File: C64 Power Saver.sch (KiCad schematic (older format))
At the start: 16 parts, among them J1 OUTPUT, J5 DIN-7, K1 SANYOU_SRD_Form_C, Q1 PN2222A, Q2 PN2222A

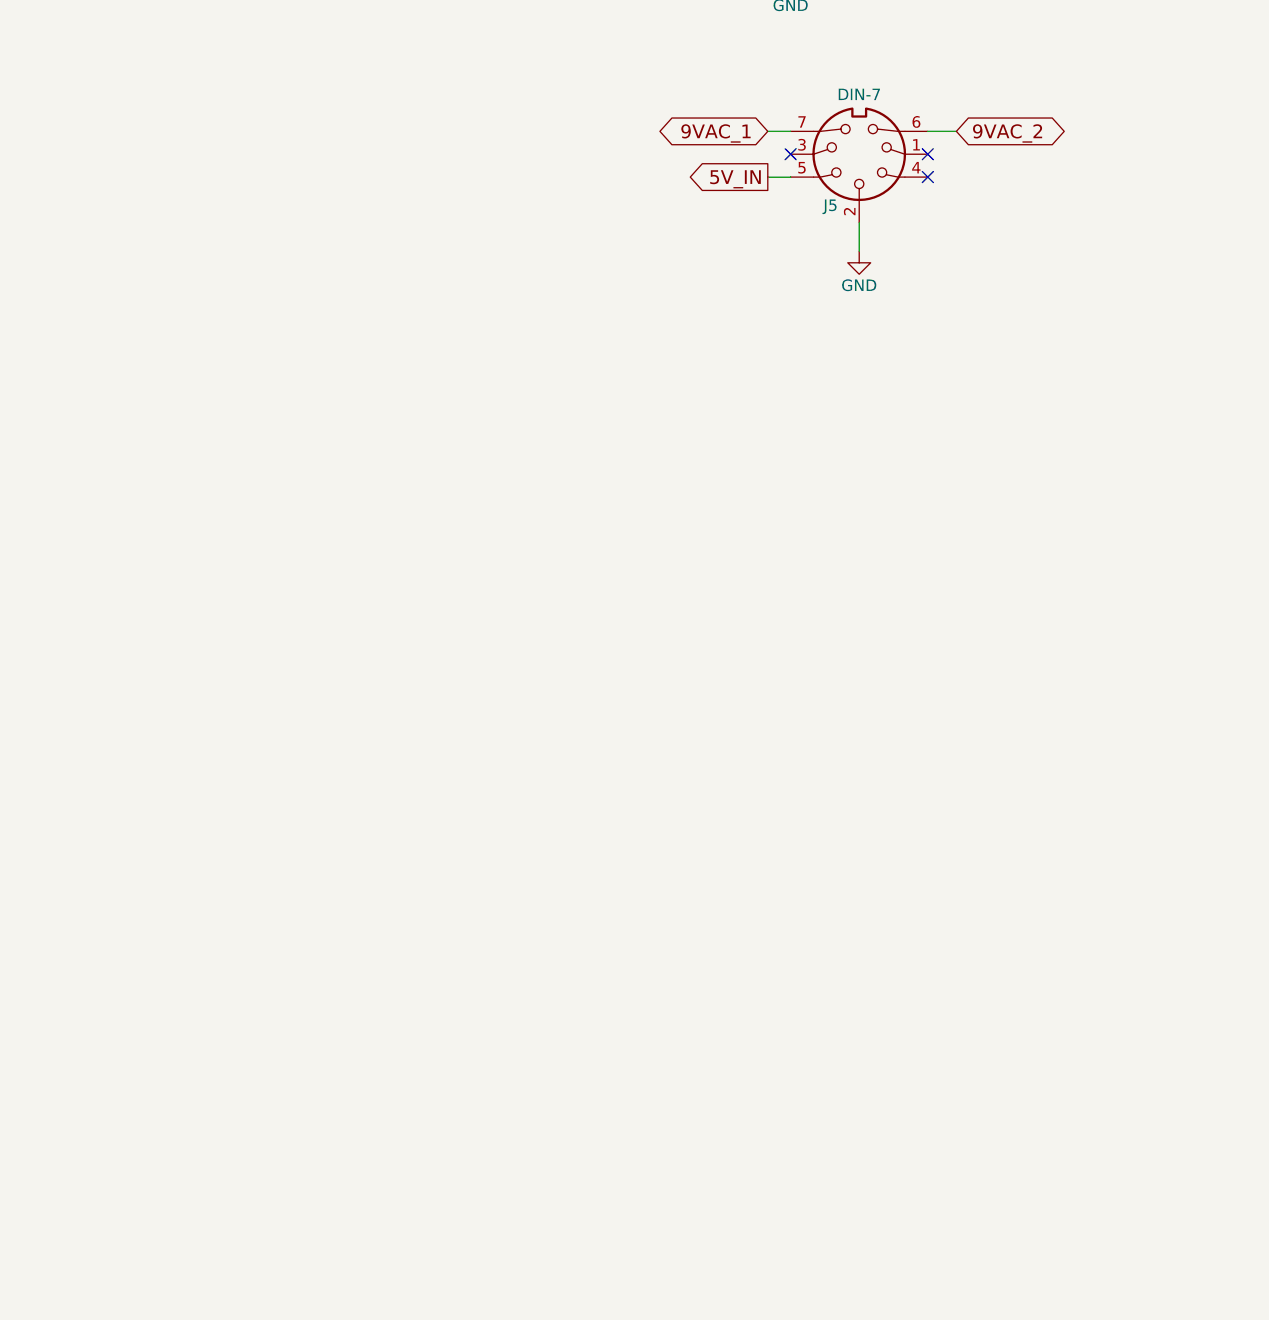
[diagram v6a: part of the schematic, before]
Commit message: Add 5v to DIN-7 pin 4
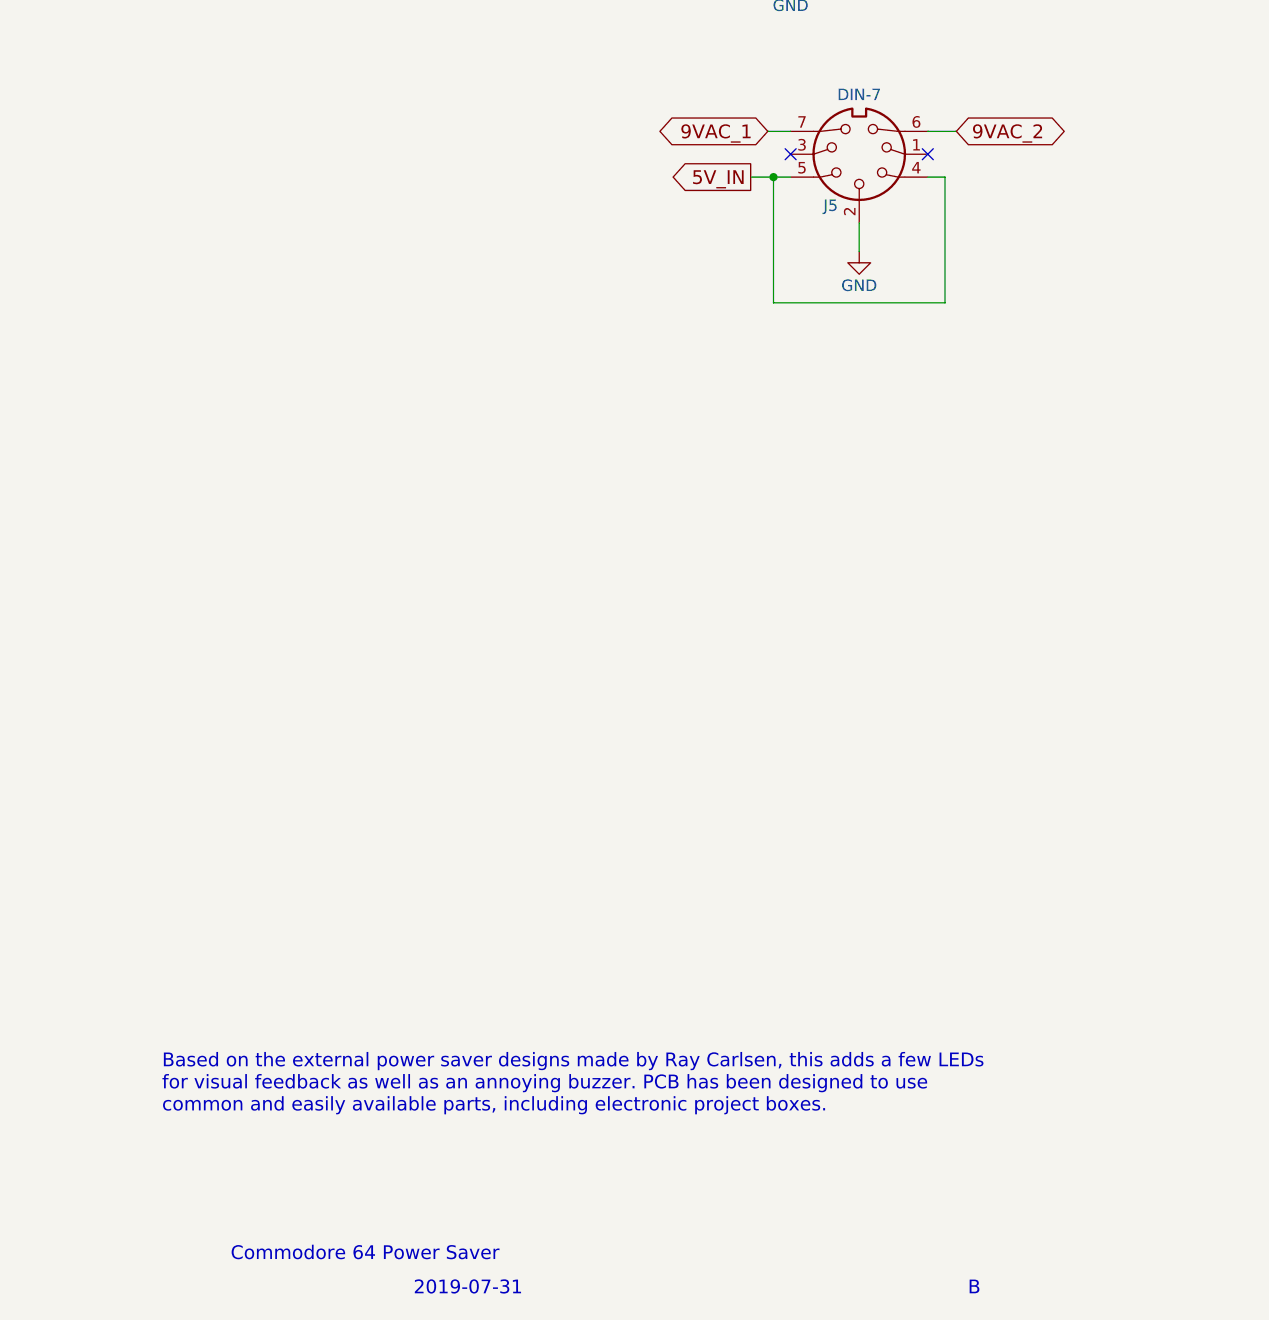
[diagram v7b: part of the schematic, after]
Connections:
- net 5V_IN: now also J5.4
- no-connect marks 3 -> 2
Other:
- note added: "2019-07-31"
- note added: "B"
- note added: "Based on the external power saver designs made by Ray Carlsen, this adds a few LEDs\nfor visual feedback as well as an annoying buzzer. PCB has been designed to use\ncommon and easily available parts, including electronic project boxes."
- note added: "Commodore 64 Power Saver"
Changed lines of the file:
@@
 NoConn ~ 10375 2650
 NoConn ~ 9775 2650
-NoConn ~ 10375 2750
-Text GLabel 9675 2750 0    60   Output ~ 0
+Text GLabel 9600 2750 0    60   Output ~ 0
 5V_IN
 Wire Wire Line
-	9675 2750 9775 2750
+	9600 2750 9775 2750
 Text GLabel 9675 2550 0    60   BiDi ~ 0
 9VAC_1
@@
 	5800 2850 5800 3900
 Connection ~ 5550 2850
+Wire Wire Line
+	9700 2750 9700 3300
+Wire Wire Line
+	9700 3300 10450 3300
+Wire Wire Line
+	10450 3300 10450 2750
+Wire Wire Line
+	10450 2750 10375 2750
+Connection ~ 9700 2750
+Text Notes 7325 7500 0    60   ~ 0
+Commodore 64 Power Saver
+Text Notes 7025 6850 0    60   ~ 0
+Based on the external power saver designs made by Ray Carlsen, this adds a few LEDs\nfor visual feedback as well as an annoying buzzer. PCB has been designed to use\ncommon and easily available parts, including electronic project boxes.
+Text Notes 10550 7650 0    60   ~ 0
+B
+Text Notes 8125 7650 0    60   ~ 0
+2019-07-31
 $EndSCHEMATC
